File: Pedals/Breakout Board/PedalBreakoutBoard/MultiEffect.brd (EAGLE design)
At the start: 61.9 x 86.3 mm, 69 parts, among them IC1 LD1117V, IC2 MCP6004P, U1 OPA1652AID

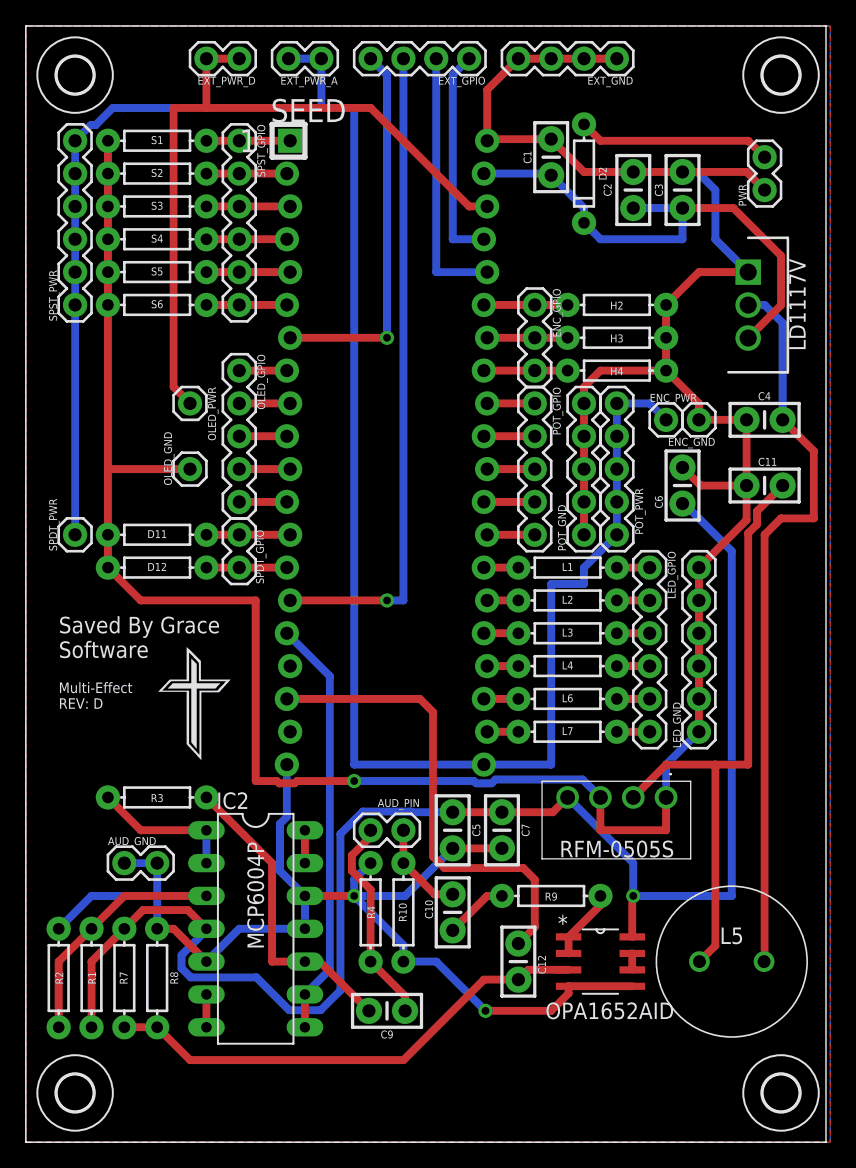
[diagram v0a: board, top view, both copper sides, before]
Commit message: DP-97 - Finish updating grounding scheme on multi-effect pedal
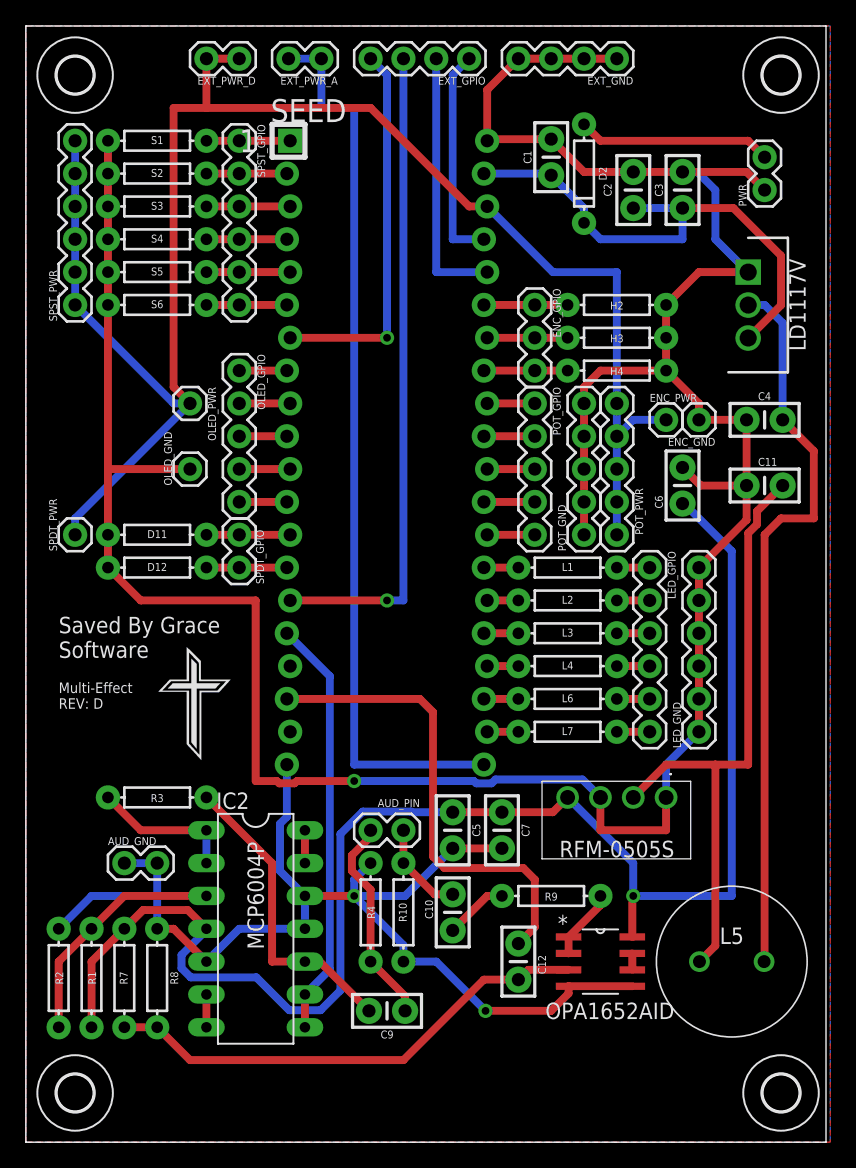
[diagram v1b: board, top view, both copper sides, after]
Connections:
- net +3V3_A: no longer ENC_PWR.1, POT_PWR.1, POT_PWR.2, POT_PWR.3, POT_PWR.4, POT_PWR.5, SPDT_PWR.1, SPST_PWR.1, SPST_PWR.2, SPST_PWR.3, SPST_PWR.4, SPST_PWR.5, SPST_PWR.6
- net +3V3_D: now also ENC_PWR.1, POT_PWR.1, POT_PWR.2, POT_PWR.3, POT_PWR.4, POT_PWR.5, SPDT_PWR.1, SPST_PWR.1, SPST_PWR.2, SPST_PWR.3, SPST_PWR.4, SPST_PWR.5, SPST_PWR.6
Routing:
- net +3V3_A: track 161.4 -> 69.7 mm
- net +3V3_D: track 57.1 -> 132.5 mm
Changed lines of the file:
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@@
 <signal name="+3V3_A">
 <contactref element="SEED" pad="21"/>
-<contactref element="SPDT_PWR" pad="1"/>
-<contactref element="ENC_PWR" pad="1"/>
 <wire x1="25.4" y1="29.21" x2="35.433" y2="29.21" width="0.6096" layer="16"/>
-<contactref element="POT_PWR" pad="1"/>
-<contactref element="POT_PWR" pad="2"/>
-<contactref element="POT_PWR" pad="3"/>
-<contactref element="POT_PWR" pad="4"/>
-<contactref element="POT_PWR" pad="5"/>
-<wire x1="45.72" y1="46.99" x2="45.72" y2="49.53" width="0.6096" layer="16"/>
-<wire x1="45.72" y1="49.53" x2="45.72" y2="52.07" width="0.6096" layer="16"/>
-<wire x1="45.72" y1="52.07" x2="45.72" y2="54.61" width="0.6096" layer="16"/>
-<wire x1="45.72" y1="54.61" x2="45.72" y2="57.15" width="0.6096" layer="16"/>
-<wire x1="45.72" y1="57.15" x2="48.26" y2="57.15" width="0.6096" layer="16"/>
-<wire x1="48.26" y1="57.15" x2="49.53" y2="55.88" width="0.6096" layer="16"/>
-<wire x1="35.433" y1="29.21" x2="40.64" y2="29.21" width="0.6096" layer="16"/>
-<wire x1="40.64" y1="29.21" x2="40.64" y2="43.18" width="0.6096" layer="16"/>
-<wire x1="40.64" y1="43.18" x2="43.18" y2="43.18" width="0.6096" layer="16"/>
-<wire x1="43.18" y1="43.18" x2="43.18" y2="44.45" width="0.6096" layer="16"/>
-<wire x1="43.18" y1="44.45" x2="45.72" y2="46.99" width="0.6096" layer="16"/>
-<contactref element="SPST_PWR" pad="1"/>
-<contactref element="SPST_PWR" pad="6"/>
-<contactref element="SPST_PWR" pad="2"/>
-<contactref element="SPST_PWR" pad="3"/>
-<contactref element="SPST_PWR" pad="4"/>
-<contactref element="SPST_PWR" pad="5"/>
-<wire x1="3.81" y1="77.47" x2="3.81" y2="74.93" width="0.6096" layer="16"/>
-<wire x1="3.81" y1="74.93" x2="3.81" y2="72.39" width="0.6096" layer="16"/>
-<wire x1="3.81" y1="72.39" x2="3.81" y2="69.85" width="0.6096" layer="16"/>
-<wire x1="3.81" y1="69.85" x2="3.81" y2="67.31" width="0.6096" layer="16"/>
-<wire x1="3.81" y1="67.31" x2="3.81" y2="64.77" width="0.6096" layer="16"/>
-<wire x1="3.81" y1="64.77" x2="3.81" y2="46.99" width="0.6096" layer="16"/>
-<wire x1="3.81" y1="77.47" x2="5.0292" y2="78.6892" width="0.6096" layer="16"/>
-<wire x1="5.0292" y1="78.6892" x2="5.4092" y2="78.6892" width="0.6096" layer="16"/>
-<wire x1="6.73" y1="80.01" x2="5.4092" y2="78.6892" width="0.6096" layer="16"/>
 <wire x1="25.4" y1="29.21" x2="25.4" y2="80.01" width="0.6096" layer="16"/>
 <wire x1="25.4" y1="80.01" x2="22.86" y2="80.01" width="0.6096" layer="16"/>
 <contactref element="EXT_PWR_A" pad="1"/>
 <contactref element="EXT_PWR_A" pad="2"/>
-<wire x1="22.86" y1="80.01" x2="6.73" y2="80.01" width="0.6096" layer="16"/>
 <wire x1="22.86" y1="80.01" x2="22.86" y2="83.82" width="0.6096" layer="16"/>
 <wire x1="22.86" y1="83.82" x2="20.32" y2="83.82" width="0.6096" layer="16"/>
@@
 <wire x1="13.97" y1="80.01" x2="13.97" y2="83.82" width="0.6096" layer="1"/>
 <wire x1="13.97" y1="83.82" x2="16.51" y2="83.82" width="0.6096" layer="1"/>
+<contactref element="SPST_PWR" pad="1"/>
+<contactref element="SPST_PWR" pad="6"/>
+<contactref element="SPST_PWR" pad="5"/>
+<contactref element="SPST_PWR" pad="4"/>
+<contactref element="SPST_PWR" pad="3"/>
+<contactref element="SPST_PWR" pad="2"/>
+<contactref element="SPDT_PWR" pad="1"/>
+<contactref element="POT_PWR" pad="1"/>
+<contactref element="POT_PWR" pad="2"/>
+<contactref element="POT_PWR" pad="3"/>
+<contactref element="POT_PWR" pad="4"/>
+<contactref element="POT_PWR" pad="5"/>
+<contactref element="ENC_PWR" pad="1"/>
+<wire x1="3.81" y1="77.47" x2="3.81" y2="74.93" width="0.6096" layer="16"/>
+<wire x1="3.81" y1="74.93" x2="3.81" y2="72.39" width="0.6096" layer="16"/>
+<wire x1="3.81" y1="72.39" x2="3.81" y2="69.85" width="0.6096" layer="16"/>
+<wire x1="3.81" y1="69.85" x2="3.81" y2="67.31" width="0.6096" layer="16"/>
+<wire x1="3.81" y1="67.31" x2="3.81" y2="64.77" width="0.6096" layer="16"/>
+<wire x1="3.81" y1="64.77" x2="11.43" y2="57.15" width="0.6096" layer="16"/>
+<wire x1="11.43" y1="57.15" x2="12.7" y2="57.15" width="0.6096" layer="16"/>
+<wire x1="12.7" y1="57.15" x2="3.81" y2="48.26" width="0.6096" layer="16"/>
+<wire x1="3.81" y1="48.26" x2="3.81" y2="46.99" width="0.6096" layer="16"/>
+<wire x1="35.687" y1="72.39" x2="40.767" y2="67.31" width="0.6096" layer="16"/>
+<wire x1="40.767" y1="67.31" x2="45.72" y2="67.31" width="0.6096" layer="16"/>
+<wire x1="45.72" y1="67.31" x2="45.72" y2="57.15" width="0.6096" layer="16"/>
+<wire x1="45.72" y1="57.15" x2="45.72" y2="54.61" width="0.6096" layer="16"/>
+<wire x1="45.72" y1="54.61" x2="45.72" y2="52.07" width="0.6096" layer="16"/>
+<wire x1="45.72" y1="52.07" x2="45.72" y2="49.53" width="0.6096" layer="16"/>
+<wire x1="45.72" y1="49.53" x2="45.72" y2="46.99" width="0.6096" layer="16"/>
+<wire x1="45.72" y1="54.61" x2="46.99" y2="55.88" width="0.6096" layer="16"/>
+<wire x1="46.99" y1="55.88" x2="49.53" y2="55.88" width="0.6096" layer="16"/>
 </signal>
 <signal name="SCL">
